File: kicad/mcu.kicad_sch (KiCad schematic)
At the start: 37 parts, among them J7 UEXT, P1 CONN_01X02, U2 STM32G431CBTx, U6 W25Q80DVS, Y1 8MHz

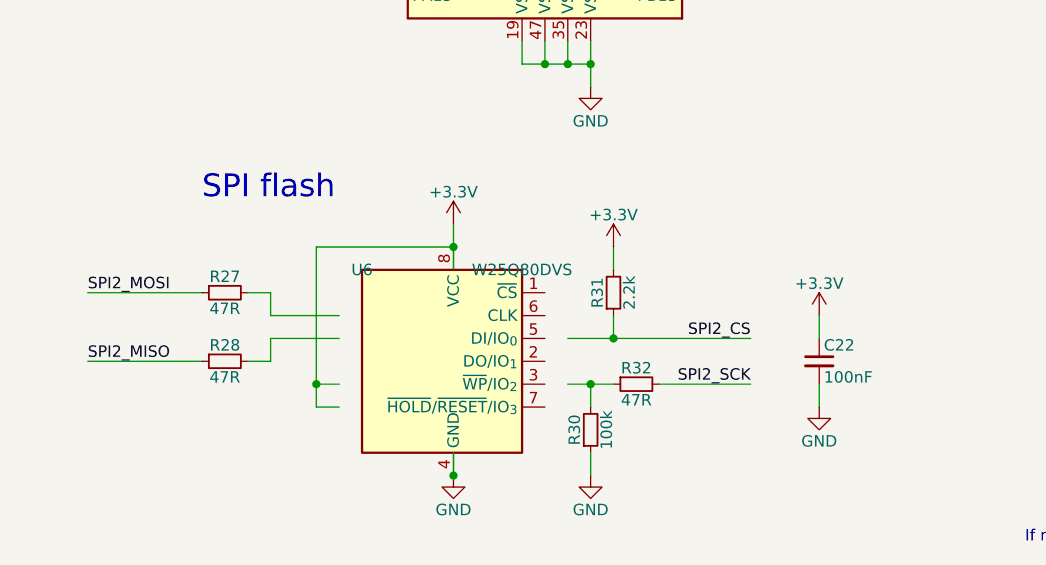
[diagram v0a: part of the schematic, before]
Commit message: Corrected MCU schematics, SPI Flash Symbol changed
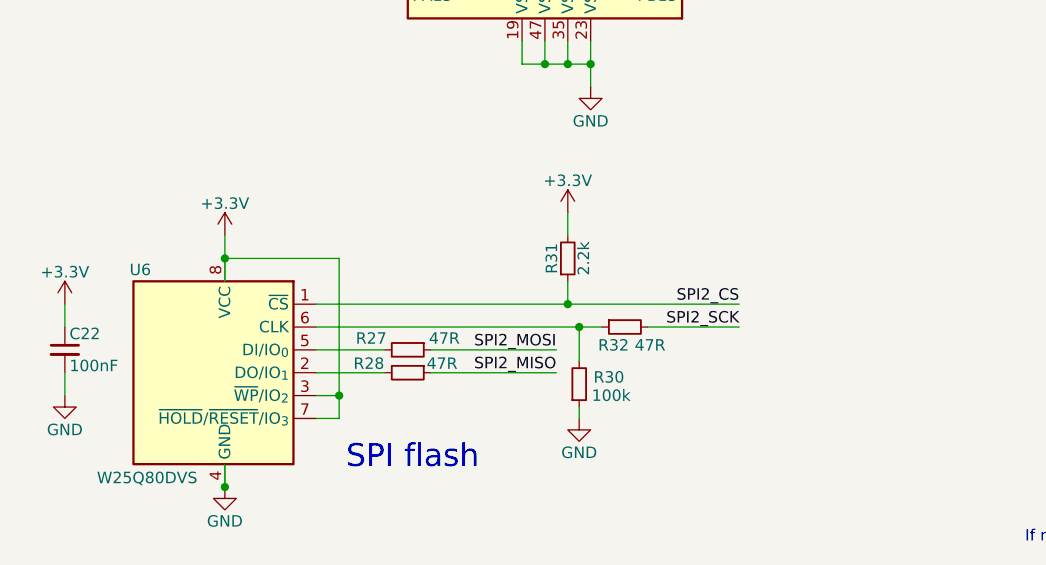
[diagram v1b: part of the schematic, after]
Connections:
- net +3.3V: now also U6.3 (~{WP}/IO_{2}), U6.7 (~{HOLD}/~{RESET}/IO_{3})
- net SPI2_CS: now also U6.1 (~{CS})
- net at U6.2 (DO/IO_{1}): now also R28.2
- net at U6.5 (DI/IO_{0}): now also R27.2
- net at U6.6 (CLK): now also R30.2, R32.1
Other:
- moved on the sheet: C22, R27, R28, R30, R31, R32, U6
